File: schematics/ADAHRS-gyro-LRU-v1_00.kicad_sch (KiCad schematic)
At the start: 7 parts

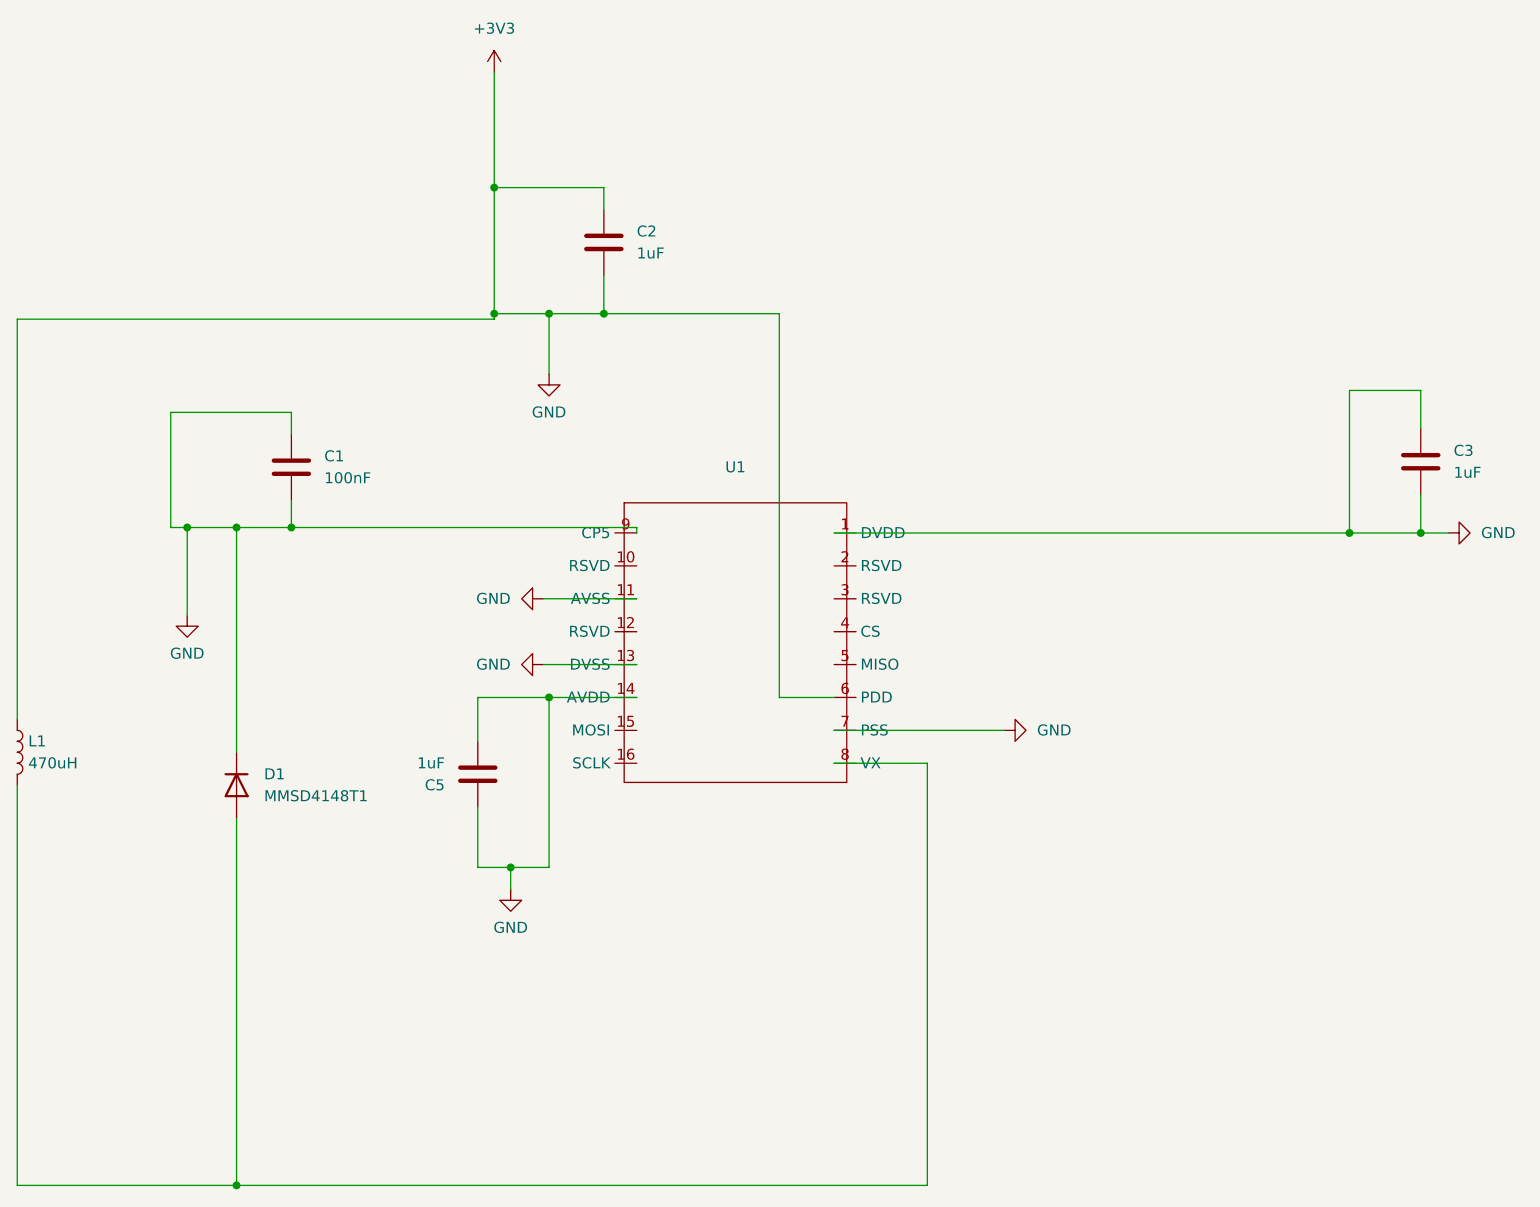
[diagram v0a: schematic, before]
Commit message: Revised v1.01
The wiring before definitely was shorting and realized I need to check back on the early designs of my schematics. I renamed and will be copying and pasting this schematic capture to get the pitch rate and the roll rate. I would like to go over the datasheet of this one to double check the circuit. Also the name of the file is not accurate and will need to rename some of these files.
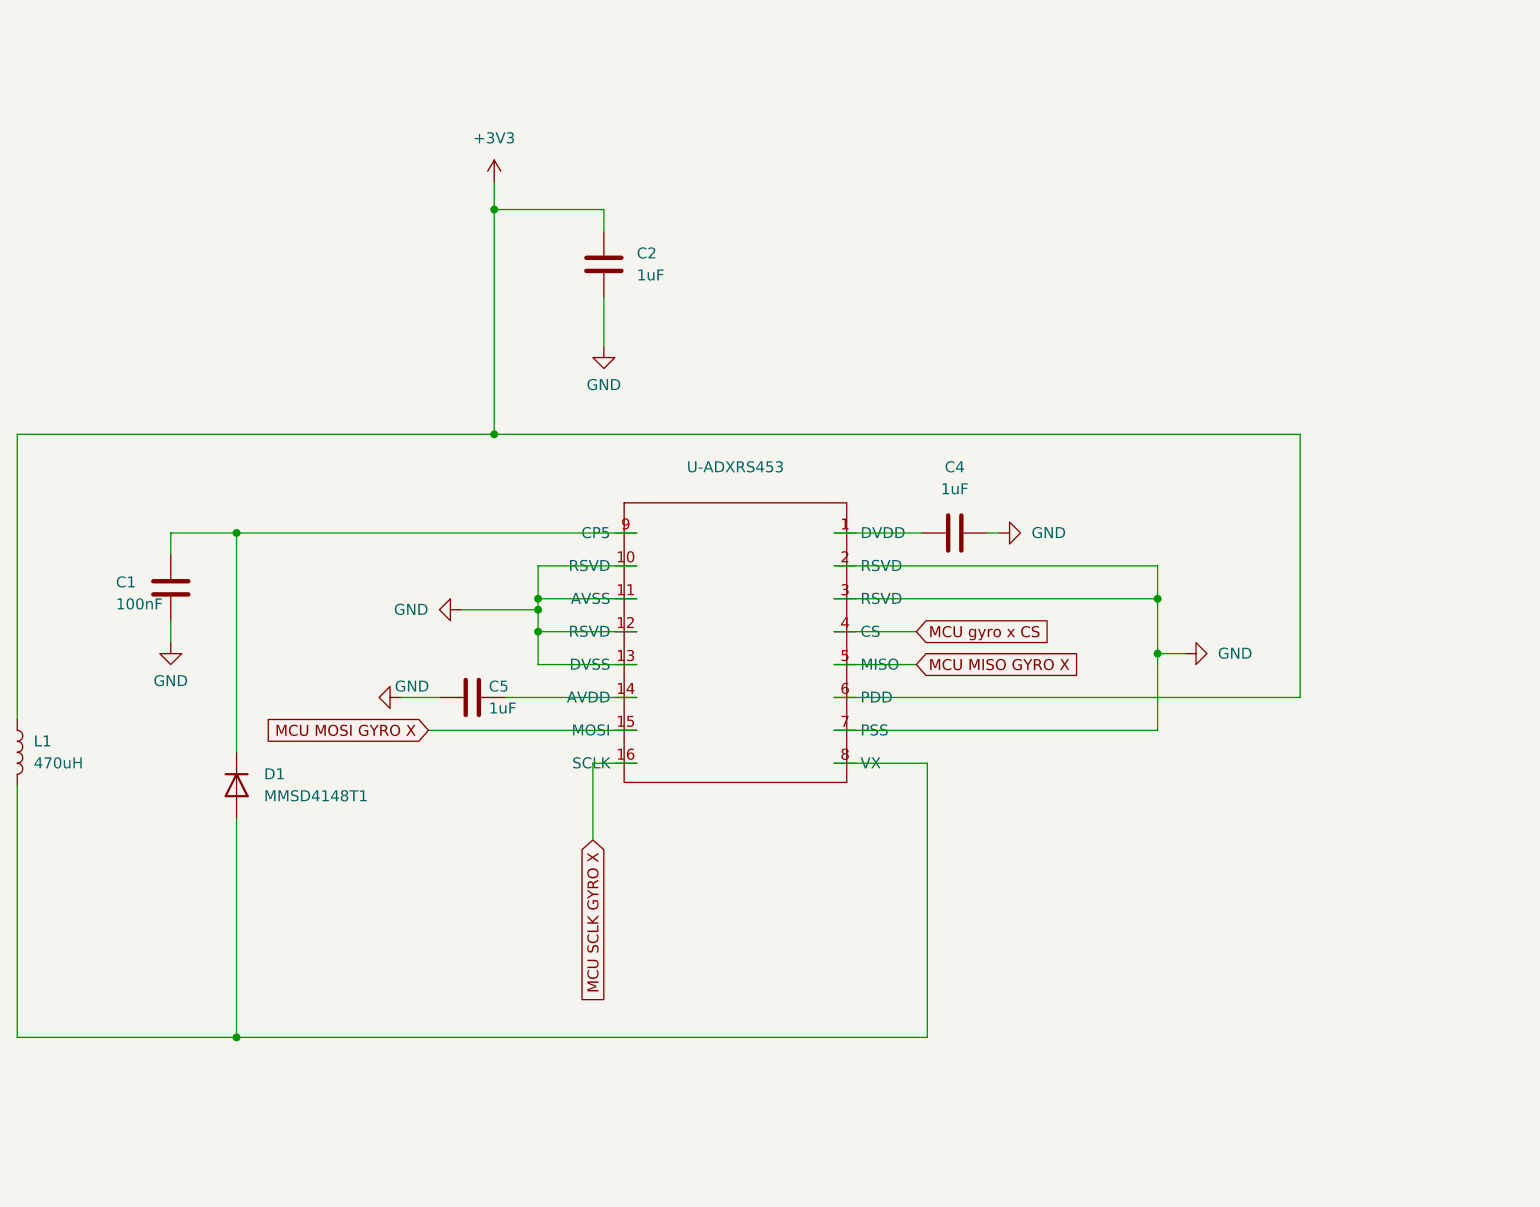
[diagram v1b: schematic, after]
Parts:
- removed C3: 1uF, symbol Device:C
- added C4: 1uF, symbol Device:C
- renumbered U1 to U-ADXRS453
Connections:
- net +3V3: no longer C1.1, C1.2, C2.2, C5.1, C5.2, D1.1 (K), U-ADXRS453.1 (DVDD), U-ADXRS453.11 (AVSS), U-ADXRS453.13 (DVSS), U-ADXRS453.14 (AVDD), U-ADXRS453.7 (PSS), U-ADXRS453.9 (CP5)
- net GND: now reaches U-ADXRS453.10 (RSVD)
- net GND: now also C1.1, C2.2, C5.1, U-ADXRS453.11 (AVSS), U-ADXRS453.12 (RSVD), U-ADXRS453.13 (DVSS), U-ADXRS453.2 (RSVD), U-ADXRS453.3 (RSVD), U-ADXRS453.7 (PSS), C4.2
- net MCU MOSI GYRO X : now reaches U-ADXRS453.15 (MOSI)
- net MCU SCLK GYRO X: now reaches U-ADXRS453.16 (SCLK)
- net MCU gyro x CS: now reaches U-ADXRS453.4 (CS)
- net MCU MISO GYRO X : now reaches U-ADXRS453.5 (MISO)
- new net: C1.2, D1.1 (K), U-ADXRS453.9 (CP5)
- new net: C4.1, U-ADXRS453.1 (DVDD)
- new net: C5.2, U-ADXRS453.14 (AVDD)
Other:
- title: ADXRS453 gyro -> ADXRS453 gyro X axis
- moved on the sheet: C1, C2, C5
